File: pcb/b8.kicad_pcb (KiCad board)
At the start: 2 copper layers, 84.6 x 36.3 mm, 30 parts, among them J1 USB, J2 ISP Programming, SW1 SW_Push, SW2 SW_Push, SW3 SW_Push, SW4 SW_Push, SW5 SW_Push, SW6 SW_Push, SW7 SW_Push, SW8 SW_Push, U1 ATtiny2313A-P, Y1 20MHz

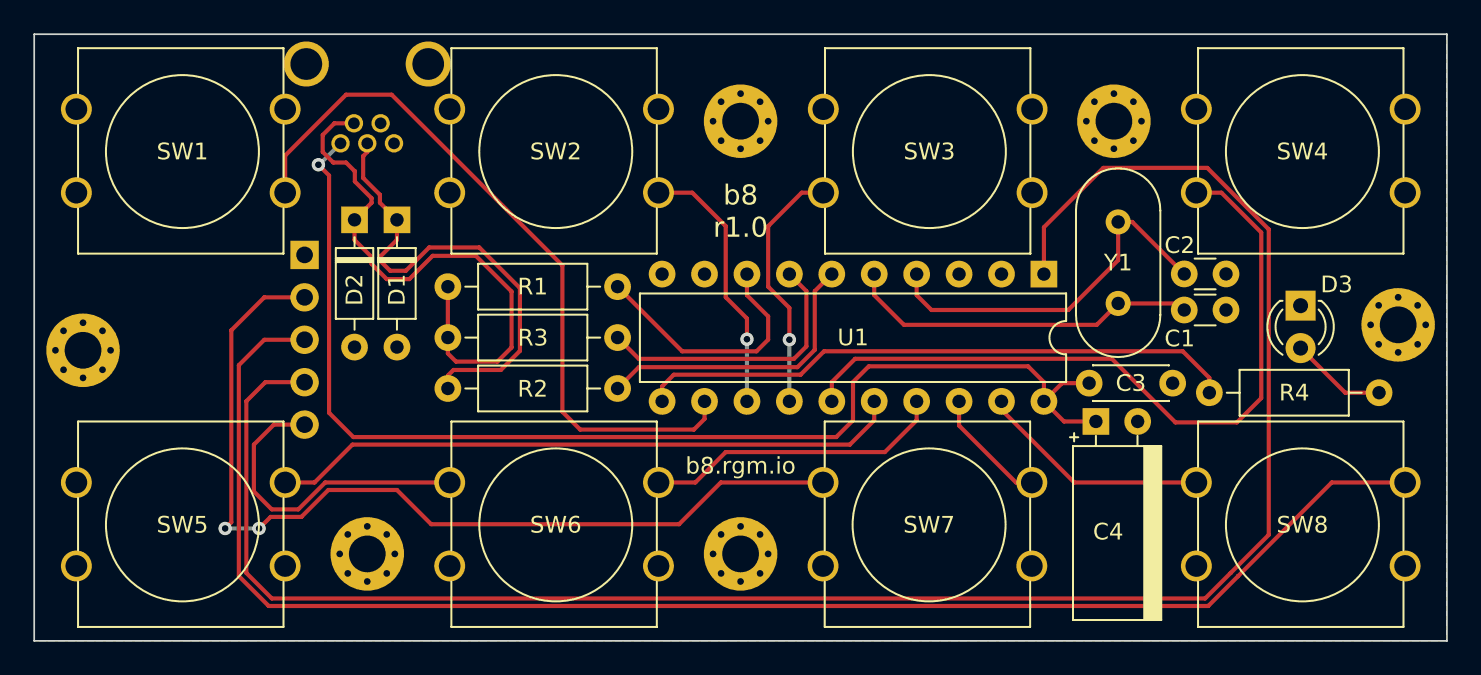
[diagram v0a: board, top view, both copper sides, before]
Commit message: pcb: revision 1.1
this revision adds a 6th pin to ISP programming header, to allow usage
of official Microchip probes, like PICKit 4. It also fixes alignment and
dimensions of the buttons.
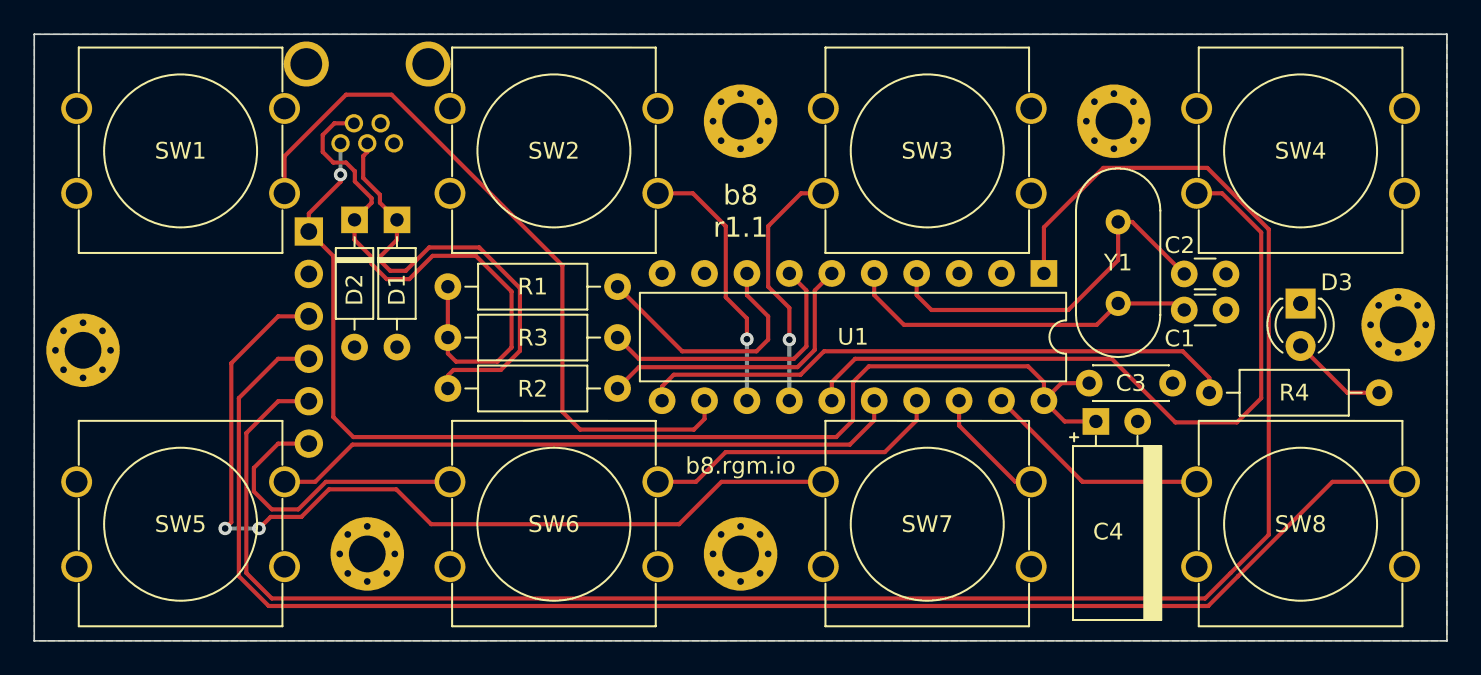
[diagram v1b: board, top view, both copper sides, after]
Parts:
- J2: footprint Connector_PinHeader_2.54mm:PinHeader_1x05_P2.54mm_Horizontal -> Connector_PinHeader_2.54mm:PinHeader_1x06_P2.54mm_Horizontal
- U1: value ATtiny2313A-P -> ATtiny4313-P
- moved J2 1.42 mm to (123.9, 75.2)
- moved REF** 0.13 mm to (183.3, 70.3)
- moved D3 0.13 mm to (183.3, 79.5)
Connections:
- J2 pad 1: GND -> +5V
- J2 pad 2: MISO -> GND
- J2 pad 3: SCK -> MISO
- J2 pad 4: RESET -> SCK
- J2 pad 5: MOSI -> RESET
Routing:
- net SCK: track 90.8 -> 89.2 mm
- net RESET: track 115.2 -> 113.6 mm
- net MISO: track 55.9 -> 54.3 mm
- net MOSI: track 19.2 -> 17.9 mm
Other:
- board text added: "b8 r1.1"
- board text removed: "b8 r1.0"
